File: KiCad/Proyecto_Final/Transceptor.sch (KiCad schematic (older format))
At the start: 51 parts, among them J2 ADC_CLK_SEL, T3 2450BL05A0100, U10 MAX2837, U9 MAX1193ETI+

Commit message: PCB MCU empezado.
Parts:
- added R13: 10k, Resistor_SMD:R_0402_1005Metric, symbol Device:R
- renumbered R13 to R14, R14 to R15, R15 to R16
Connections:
- net labels added: PD0_adc, PD1_adc
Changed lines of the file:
@@
 	4250 3150 4350 3150
 $Comp
-L power:GND #PWR070
+L power:GND #PWR071
 U 1 1 5FDBB07B
 P 4250 3250
-F 0 "#PWR070" H 4250 3000 50  0001 C CNN
+F 0 "#PWR071" H 4250 3000 50  0001 C CNN
 F 1 "GND" V 4255 3122 50  0000 R CNN
 F 2 "" H 4250 3250 50  0001 C CNN
@@
 	4250 3250 4350 3250
 $Comp
-L power:GND #PWR063
+L power:GND #PWR064
 U 1 1 5FDC599C
 P 1850 2750
-F 0 "#PWR063" H 1850 2500 50  0001 C CNN
+F 0 "#PWR064" H 1850 2500 50  0001 C CNN
 F 1 "GND" H 1855 2577 50  0000 C CNN
 F 2 "" H 1850 2750 50  0001 C CNN
@@
 $EndComp
 $Comp
-L power:GND #PWR067
+L power:GND #PWR068
 U 1 1 5FF7C6C8
 P 3850 2950
-F 0 "#PWR067" H 3850 2700 50  0001 C CNN
+F 0 "#PWR068" H 3850 2700 50  0001 C CNN
 F 1 "GND" H 3855 2777 50  0000 C CNN
 F 2 "" H 3850 2950 50  0001 C CNN
@@
 $EndComp
 $Comp
-L power:GND #PWR073
+L power:GND #PWR074
 U 1 1 602890BB
 P 3700 4100
-F 0 "#PWR073" H 3700 3850 50  0001 C CNN
+F 0 "#PWR074" H 3700 3850 50  0001 C CNN
 F 1 "GND" H 3705 3927 50  0000 C CNN
 F 2 "" H 3700 4100 50  0001 C CNN
@@
 	5650 5350 5650 5450
 $Comp
-L power:GND #PWR080
+L power:GND #PWR081
 U 1 1 602ED381
 P 5650 5950
-F 0 "#PWR080" H 5650 5700 50  0001 C CNN
+F 0 "#PWR081" H 5650 5700 50  0001 C CNN
 F 1 "GND" H 5655 5777 50  0000 C CNN
 F 2 "" H 5650 5950 50  0001 C CNN
@@
 $EndComp
 $Comp
-L power:GND #PWR081
+L power:GND #PWR082
 U 1 1 602F5473
 P 6050 5950
-F 0 "#PWR081" H 6050 5700 50  0001 C CNN
+F 0 "#PWR082" H 6050 5700 50  0001 C CNN
 F 1 "GND" H 6055 5777 50  0000 C CNN
 F 2 "" H 6050 5950 50  0001 C CNN
@@
 	6800 5450 6800 5500
 $Comp
-L power:GND #PWR082
+L power:GND #PWR083
 U 1 1 6030B87C
 P 6400 5950
-F 0 "#PWR082" H 6400 5700 50  0001 C CNN
+F 0 "#PWR083" H 6400 5700 50  0001 C CNN
 F 1 "GND" H 6405 5777 50  0000 C CNN
 F 2 "" H 6400 5950 50  0001 C CNN
@@
 	5700 5000 5700 5350
 $Comp
-L power:GND #PWR078
+L power:GND #PWR079
 U 1 1 6031E78A
 P 6000 5100
-F 0 "#PWR078" H 6000 4850 50  0001 C CNN
+F 0 "#PWR079" H 6000 4850 50  0001 C CNN
 F 1 "GND" H 6005 4927 50  0000 C CNN
 F 2 "" H 6000 5100 50  0001 C CNN
@@
 $EndComp
 $Comp
-L Device:R R14
+L Device:R R15
 U 1 1 603235A8
 P 7400 5450
-F 0 "R14" V 7193 5450 50  0000 C CNN
+F 0 "R15" V 7193 5450 50  0000 C CNN
 F 1 "475" V 7284 5450 50  0000 C CNN
 F 2 "Resistor_SMD:R_0402_1005Metric" V 7330 5450 50  0001 C CNN
@@
 $EndComp
 $Comp
-L Device:R R15
+L Device:R R16
 U 1 1 60324995
 P 7900 5450
-F 0 "R15" V 7693 5450 50  0000 C CNN
+F 0 "R16" V 7693 5450 50  0000 C CNN
 F 1 "475" V 7784 5450 50  0000 C CNN
 F 2 "Resistor_SMD:R_0402_1005Metric" V 7830 5450 50  0001 C CNN
@@
 Trx_Enable
 $Comp
-L power:GND #PWR076
+L power:GND #PWR077
 U 1 1 60342D46
 P 7100 4750
-F 0 "#PWR076" H 7100 4500 50  0001 C CNN
+F 0 "#PWR077" H 7100 4500 50  0001 C CNN
 F 1 "GND" H 7105 4577 50  0000 C CNN
 F 2 "" H 7100 4750 50  0001 C CNN
@@
 	7350 4050 6950 4050
 $Comp
-L power:GND #PWR075
+L power:GND #PWR076
 U 1 1 6034C833
 P 7350 4450
-F 0 "#PWR075" H 7350 4200 50  0001 C CNN
+F 0 "#PWR076" H 7350 4200 50  0001 C CNN
 F 1 "GND" H 7355 4277 50  0000 C CNN
 F 2 "" H 7350 4450 50  0001 C CNN
@@
 $EndComp
 $Comp
-L power:GND #PWR074
+L power:GND #PWR075
 U 1 1 6035D352
 P 7750 4250
-F 0 "#PWR074" H 7750 4000 50  0001 C CNN
+F 0 "#PWR075" H 7750 4000 50  0001 C CNN
 F 1 "GND" H 7755 4077 50  0000 C CNN
 F 2 "" H 7750 4250 50  0001 C CNN
@@
 $EndComp
 $Comp
-L power:GND #PWR069
+L power:GND #PWR070
 U 1 1 60414246
 P 11150 3100
-F 0 "#PWR069" H 11150 2850 50  0001 C CNN
+F 0 "#PWR070" H 11150 2850 50  0001 C CNN
 F 1 "GND" H 11155 2927 50  0000 C CNN
 F 2 "" H 11150 3100 50  0001 C CNN
@@
 	11400 3550 11500 3550
 $Comp
-L power:GND #PWR072
+L power:GND #PWR073
 U 1 1 60440365
 P 11700 3850
-F 0 "#PWR072" H 11700 3600 50  0001 C CNN
+F 0 "#PWR073" H 11700 3600 50  0001 C CNN
 F 1 "GND" H 11705 3677 50  0000 C CNN
 F 2 "" H 11700 3850 50  0001 C CNN
@@
 $EndComp
 $Comp
-L power:GND #PWR066
+L power:GND #PWR067
 U 1 1 604A2502
 P 15000 2850
-F 0 "#PWR066" H 15000 2600 50  0001 C CNN
+F 0 "#PWR067" H 15000 2600 50  0001 C CNN
 F 1 "GND" H 15005 2677 50  0000 C CNN
 F 2 "" H 15000 2850 50  0001 C CNN
@@
 $EndComp
 $Comp
-L power:GND #PWR071
+L power:GND #PWR072
 U 1 1 60506EB7
 P 14950 3250
-F 0 "#PWR071" H 14950 3000 50  0001 C CNN
+F 0 "#PWR072" H 14950 3000 50  0001 C CNN
 F 1 "GND" H 14955 3077 50  0000 C CNN
 F 2 "" H 14950 3250 50  0001 C CNN
@@
 CLK_ADC
 $Comp
-L power:GND #PWR064
+L power:GND #PWR065
 U 1 1 6030CF99
 P 4350 2800
-F 0 "#PWR064" H 4350 2550 50  0001 C CNN
+F 0 "#PWR065" H 4350 2550 50  0001 C CNN
 F 1 "GND" V 4355 2672 50  0000 R CNN
 F 2 "" H 4350 2800 50  0001 C CNN
@@
 Connection ~ 3700 3750
 $Comp
-L Device:R R13
+L Device:R R14
 U 1 1 60373025
 P 4000 4100
-F 0 "R13" H 4200 4100 50  0000 R CNN
+F 0 "R14" H 4200 4100 50  0000 R CNN
 F 1 "100" V 4000 4150 50  0000 R CNN
 F 2 "Resistor_SMD:R_0402_1005Metric" V 3930 4100 50  0001 C CNN
@@
 	5300 1100 5300 2400
 $Comp
-L power:GND #PWR065
+L power:GND #PWR066
 U 1 1 603671E8
 P 12300 2850
-F 0 "#PWR065" H 12300 2600 50  0001 C CNN
+F 0 "#PWR066" H 12300 2600 50  0001 C CNN
 F 1 "GND" V 12305 2677 50  0000 C CNN
 F 2 "" H 12300 2850 50  0001 C CNN
@@
 $EndComp
 $Comp
-L power:GND #PWR068
+L power:GND #PWR069
 U 1 1 60367BE1
 P 12300 2950
-F 0 "#PWR068" H 12300 2700 50  0001 C CNN
+F 0 "#PWR069" H 12300 2700 50  0001 C CNN
 F 1 "GND" V 12305 2777 50  0000 C CNN
 F 2 "" H 12300 2950 50  0001 C CNN
@@
 D0
 Text GLabel 13900 2650 2    50   Input ~ 0
-PD1
+PD1_adc
 Text GLabel 13900 2550 2    50   Input ~ 0
-PD0
+PD0_adc
 $Comp
 L power:GND #PWR057
@@
 $EndComp
 $Comp
-L power:GND #PWR079
+L power:GND #PWR080
 U 1 1 60757CE4
 P 4900 5400
-F 0 "#PWR079" H 4900 5150 50  0001 C CNN
+F 0 "#PWR080" H 4900 5150 50  0001 C CNN
 F 1 "GND" H 4905 5227 50  0000 C CNN
 F 2 "" H 4900 5400 50  0001 C CNN
@@
 VDD
 $Comp
-L power:+3.3V #PWR077
+L power:+3.3V #PWR078
 U 1 1 60750D11
 P 10500 5000
-F 0 "#PWR077" H 10500 4850 50  0001 C CNN
+F 0 "#PWR078" H 10500 4850 50  0001 C CNN
 F 1 "+3.3V" H 10515 5173 50  0000 C CNN
 F 2 "" H 10500 5000 50  0001 C CNN
@@
 Text Label 4100 3550 2    50   ~ 0
 RXRF-
+Text GLabel 8000 2900 3    50   Input ~ 0
+SPI1_CS1
+$Comp
+L Device:R R13
+U 1 1 60912B2D
+P 8000 2750
+F 0 "R13" H 8070 2796 50  0000 L CNN
+F 1 "10k" H 8070 2705 50  0000 L CNN
+F 2 "Resistor_SMD:R_0402_1005Metric" V 7930 2750 50  0001 C CNN
+F 3 "~" H 8000 2750 50  0001 C CNN
+	1    8000 2750
+	1    0    0    -1
+$EndComp
+$Comp
+L power:+3.3V #PWR063
+U 1 1 609150E8
+P 8000 2600
+F 0 "#PWR063" H 8000 2450 50  0001 C CNN
+F 1 "+3.3V" H 8015 2773 50  0000 C CNN
+F 2 "" H 8000 2600 50  0001 C CNN
+F 3 "" H 8000 2600 50  0001 C CNN
+	1    8000 2600
+	1    0    0    -1
+$EndComp
 $EndSCHEMATC

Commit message: Reasignación de footprints por cambio de proveedor de componentes (JLCPCB SMT Assembly).
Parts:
- C51: footprint Capacitor_SMD:C_0805_2012Metric -> Capacitor_SMD:C_0603_1608Metric
- C52, C54, C61, C64: value 0.1uF -> 100nF
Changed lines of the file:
@@
 P 11350 2200
 F 0 "C52" V 11098 2200 50  0000 C CNN
-F 1 "0.1uF" V 11189 2200 50  0000 C CNN
+F 1 "100nF" V 11189 2200 50  0000 C CNN
 F 2 "Capacitor_SMD:C_0402_1005Metric" H 11388 2050 50  0001 C CNN
 F 3 "~" H 11350 2200 50  0001 C CNN
@@
 F 0 "C51" V 10698 2200 50  0000 C CNN
 F 1 "2.2uF" V 10789 2200 50  0000 C CNN
-F 2 "Capacitor_SMD:C_0805_2012Metric" H 10988 2050 50  0001 C CNN
+F 2 "Capacitor_SMD:C_0603_1608Metric" H 10988 2050 50  0001 C CNN
 F 3 "~" H 10950 2200 50  0001 C CNN
 	1    10950 2200
@@
 P 11350 2950
 F 0 "C61" V 11098 2950 50  0000 C CNN
-F 1 "0.1uF" V 11189 2950 50  0000 C CNN
+F 1 "100nF" V 11189 2950 50  0000 C CNN
 F 2 "Capacitor_SMD:C_0402_1005Metric" H 11388 2800 50  0001 C CNN
 F 3 "~" H 11350 2950 50  0001 C CNN
@@
 P 11900 3700
 F 0 "C64" V 11648 3700 50  0000 C CNN
-F 1 "0.1uF" V 11739 3700 50  0000 C CNN
+F 1 "100nF" V 11739 3700 50  0000 C CNN
 F 2 "Capacitor_SMD:C_0402_1005Metric" H 11938 3550 50  0001 C CNN
 F 3 "~" H 11900 3700 50  0001 C CNN
@@
 P 15300 2200
 F 0 "C54" V 15048 2200 50  0000 C CNN
-F 1 "0.1uF" V 15139 2200 50  0000 C CNN
+F 1 "100nF" V 15139 2200 50  0000 C CNN
 F 2 "Capacitor_SMD:C_0402_1005Metric" H 15338 2050 50  0001 C CNN
 F 3 "~" H 15300 2200 50  0001 C CNN

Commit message: Sección RF terminada.
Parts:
- removed J2: ADC_CLK_SEL, Connector_PinHeader_2.54mm:PinHeader_2x02_P2.54mm_Vertical_SMD, symbol Connector_Generic:Conn_02x02_Counter_Clockwise
- removed R13: 10k, Resistor_SMD:R_0402_1005Metric, symbol Device:R
- renumbered R11 to R10, R12 to R11, R14 to R12, R15 to R13, R16 to R14, R8 to R7, R9 to R8, R10 to R9
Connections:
- net labels removed: ADC_22MHz, ADC_45MHz
- wire segments 148 -> 144

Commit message: Avances PCB.
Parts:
- renumbered C48 to C1, C57 to C10, C58 to C11, C59 to C12, C60 to C13, C61 to C14, C62 to C15, C63 to C16, C64 to C17, C65 to C18, C66 to C19, C49 to C2, C67 to C20, C68 to C21, C69 to C22, C70 to C23, C71 to C24, C72 to C25, C73 to C26, C74 to C27, C50 to C3, C51 to C4, C52 to C5, C53 to C6, C54 to C7, C55 to C8, C56 to C9, L4 to L1, R7 to R1, R8 to R2, R9 to R3, R10 to R4, R11 to R5, R12 to R6, R13 to R7, R14 to R8, T3 to T1, U9 to U1, U10 to U2

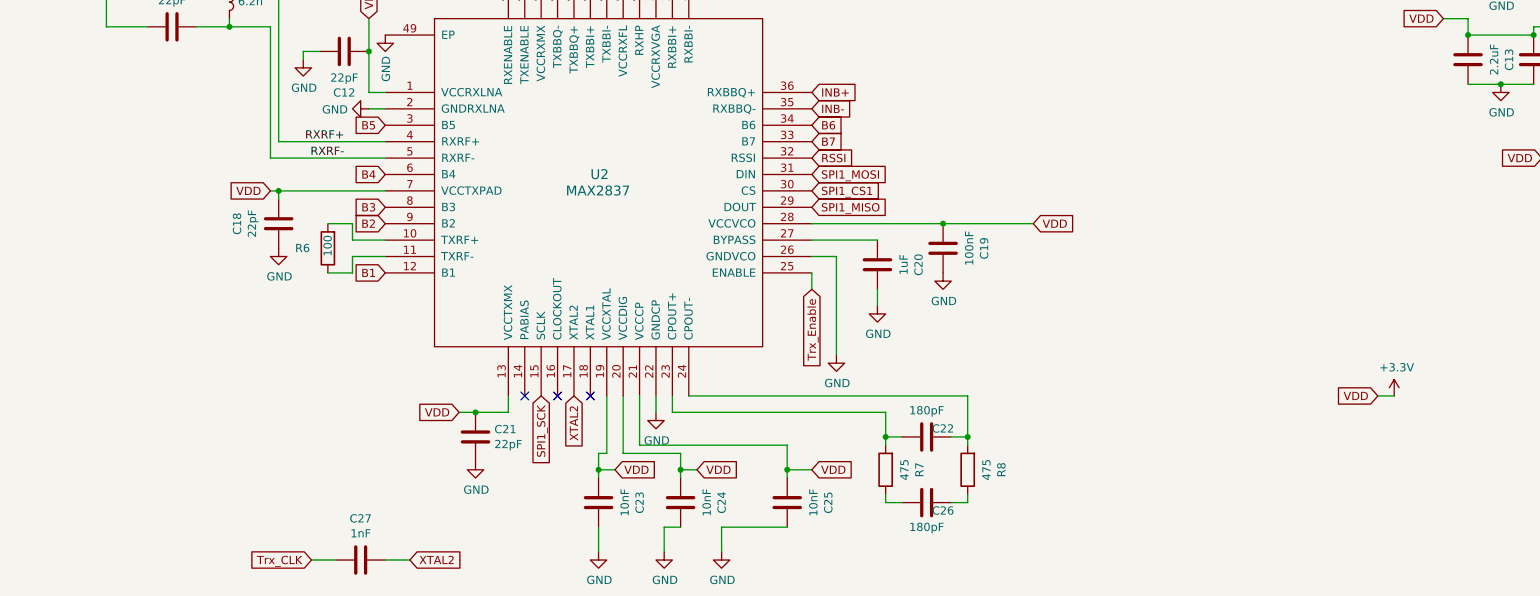
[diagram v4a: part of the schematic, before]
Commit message: Eliminadas conexiones innecesarias del transceptor.
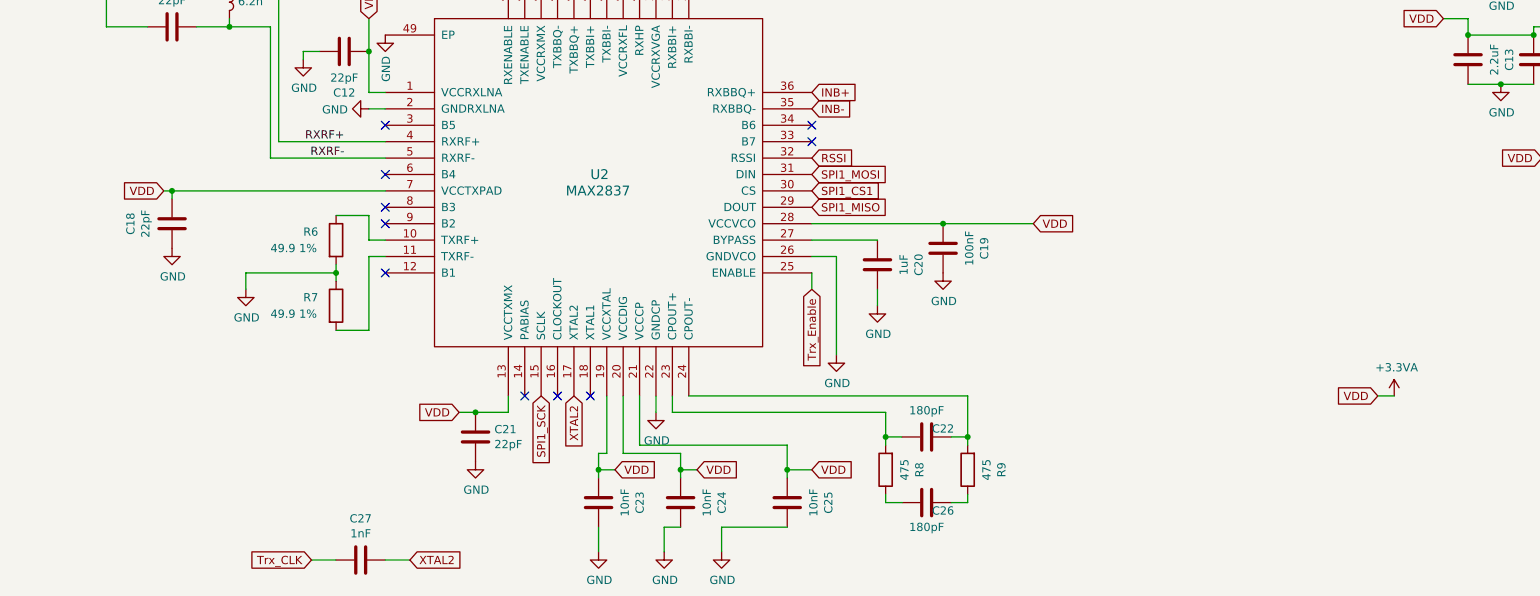
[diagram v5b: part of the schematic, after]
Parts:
- added R7: 49.9 1%, Resistor_SMD:R_0402_1005Metric, symbol Device:R
- R6: value 100 -> 49.9 1%
- renumbered R7 to R8, R8 to R9
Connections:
- net GND: now also R6.2, R7.1
- net at U2.10 (TXRF+): now also R6.1; no longer R6.2
- net at U2.11 (TXRF-): now also R7.2; no longer R6.1
- net +3V3 renamed +3.3VA
- net B1: no longer names the net of U2.12 (B1)
- net B2: no longer names the net of U2.9 (B2)
- net B3: no longer names the net of U2.8 (B3)
- net B4: no longer names the net of U2.6 (B4)
- net B5: no longer names the net of U2.3 (B5)
- net B6: no longer names the net of U2.34 (B6)
- net B7: no longer names the net of U2.33 (B7)
- no-connect marks 4 -> 11
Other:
- moved on the sheet: C18
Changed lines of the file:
@@
 L Device:C C18
 U 1 1 602785CE
-P 3700 3950
-F 0 "C18" V 3448 3950 50  0000 C CNN
-F 1 "22pF" V 3539 3950 50  0000 C CNN
-F 2 "Capacitor_SMD:C_0402_1005Metric" H 3738 3800 50  0001 C CNN
-F 3 "~" H 3700 3950 50  0001 C CNN
-	1    3700 3950
+P 3050 3950
+F 0 "C18" V 2798 3950 50  0000 C CNN
+F 1 "22pF" V 2889 3950 50  0000 C CNN
+F 2 "Capacitor_SMD:C_0402_1005Metric" H 3088 3800 50  0001 C CNN
+F 3 "~" H 3050 3950 50  0001 C CNN
+	1    3050 3950
 	1    0    0    -1
 $EndComp
@@
 L power:GND #PWR024
 U 1 1 602890BB
-P 3700 4100
-F 0 "#PWR024" H 3700 3850 50  0001 C CNN
-F 1 "GND" H 3705 3927 50  0000 C CNN
-F 2 "" H 3700 4100 50  0001 C CNN
-F 3 "" H 3700 4100 50  0001 C CNN
-	1    3700 4100
+P 3050 4100
+F 0 "#PWR024" H 3050 3850 50  0001 C CNN
+F 1 "GND" H 3055 3927 50  0000 C CNN
+F 2 "" H 3050 4100 50  0001 C CNN
+F 3 "" H 3050 4100 50  0001 C CNN
+	1    3050 4100
 	1    0    0    -1
 $EndComp
@@
 	5650 5350 5650 5450
 $Comp
-L power:GND #PWR031
+L power:GND #PWR032
 U 1 1 602ED381
 P 5650 5950
-F 0 "#PWR031" H 5650 5700 50  0001 C CNN
+F 0 "#PWR032" H 5650 5700 50  0001 C CNN
 F 1 "GND" H 5655 5777 50  0000 C CNN
 F 2 "" H 5650 5950 50  0001 C CNN
@@
 $EndComp
 $Comp
-L power:GND #PWR032
+L power:GND #PWR033
 U 1 1 602F5473
 P 6050 5950
-F 0 "#PWR032" H 6050 5700 50  0001 C CNN
+F 0 "#PWR033" H 6050 5700 50  0001 C CNN
 F 1 "GND" H 6055 5777 50  0000 C CNN
 F 2 "" H 6050 5950 50  0001 C CNN
@@
 	6800 5450 6800 5500
 $Comp
-L power:GND #PWR033
+L power:GND #PWR034
 U 1 1 6030B87C
 P 6400 5950
-F 0 "#PWR033" H 6400 5700 50  0001 C CNN
+F 0 "#PWR034" H 6400 5700 50  0001 C CNN
 F 1 "GND" H 6405 5777 50  0000 C CNN
 F 2 "" H 6400 5950 50  0001 C CNN
@@
 	5700 5000 5700 5350
 $Comp
-L power:GND #PWR029
+L power:GND #PWR030
 U 1 1 6031E78A
 P 6000 5100
-F 0 "#PWR029" H 6000 4850 50  0001 C CNN
+F 0 "#PWR030" H 6000 4850 50  0001 C CNN
 F 1 "GND" H 6005 4927 50  0000 C CNN
 F 2 "" H 6000 5100 50  0001 C CNN
@@
 $EndComp
 $Comp
-L Device:R R7
+L Device:R R8
 U 1 1 603235A8
 P 7400 5450
-F 0 "R7" V 7193 5450 50  0000 C CNN
+F 0 "R8" V 7193 5450 50  0000 C CNN
 F 1 "475" V 7284 5450 50  0000 C CNN
 F 2 "Resistor_SMD:R_0402_1005Metric" V 7330 5450 50  0001 C CNN
@@
 $EndComp
 $Comp
-L Device:R R8
+L Device:R R9
 U 1 1 60324995
 P 7900 5450
-F 0 "R8" V 7693 5450 50  0000 C CNN
+F 0 "R9" V 7693 5450 50  0000 C CNN
 F 1 "475" V 7784 5450 50  0000 C CNN
 F 2 "Resistor_SMD:R_0402_1005Metric" V 7830 5450 50  0001 C CNN
@@
 Trx_Enable
 $Comp
-L power:GND #PWR027
+L power:GND #PWR028
 U 1 1 60342D46
 P 7100 4750
-F 0 "#PWR027" H 7100 4500 50  0001 C CNN
+F 0 "#PWR028" H 7100 4500 50  0001 C CNN
 F 1 "GND" H 7105 4577 50  0000 C CNN
 F 2 "" H 7100 4750 50  0001 C CNN
@@
 	7350 4050 6950 4050
 $Comp
-L power:GND #PWR026
+L power:GND #PWR027
 U 1 1 6034C833
 P 7350 4450
-F 0 "#PWR026" H 7350 4200 50  0001 C CNN
+F 0 "#PWR027" H 7350 4200 50  0001 C CNN
 F 1 "GND" H 7355 4277 50  0000 C CNN
 F 2 "" H 7350 4450 50  0001 C CNN
@@
 	1    0    0    -1
 $EndComp
-Text GLabel 3650 3750 0    50   Input ~ 0
+Text GLabel 3000 3750 0    50   Input ~ 0
 VDD
 Text GLabel 4250 2700 1    50   Input ~ 0
@@
 Connection ~ 4250 2900
 Wire Wire Line
-	3650 3750 3700 3750
-Wire Wire Line
-	3700 3800 3700 3750
-Connection ~ 3700 3750
-$Comp
-L Device:R R6
-U 1 1 60373025
-P 4000 4100
-F 0 "R6" H 4200 4100 50  0000 R CNN
-F 1 "100" V 4000 4150 50  0000 R CNN
-F 2 "Resistor_SMD:R_0402_1005Metric" V 3930 4100 50  0001 C CNN
-F 3 "~" H 4000 4100 50  0001 C CNN
-	1    4000 4100
-	-1   0    0    1
-$EndComp
+	3000 3750 3050 3750
+Wire Wire Line
+	3050 3800 3050 3750
+Connection ~ 3050 3750
 NoConn ~ 5200 5000
 $Comp
@@
 $EndComp
 $Comp
-L power:GND #PWR030
+L power:GND #PWR031
 U 1 1 60757CE4
 P 4900 5400
-F 0 "#PWR030" H 4900 5150 50  0001 C CNN
+F 0 "#PWR031" H 4900 5150 50  0001 C CNN
 F 1 "GND" H 4905 5227 50  0000 C CNN
 F 2 "" H 4900 5400 50  0001 C CNN
@@
 Text GLabel 5900 2400 1    50   Input ~ 0
 RXHP
-Text GLabel 4350 3350 0    50   Input ~ 0
-B5
-Text GLabel 4350 3650 0    50   Input ~ 0
-B4
-Text GLabel 4350 3850 0    50   Input ~ 0
-B3
-Text GLabel 4350 3950 0    50   Input ~ 0
-B2
-Wire Wire Line
-	3700 3750 4350 3750
-Wire Wire Line
-	4350 4050 4150 4050
-Wire Wire Line
-	4150 4050 4150 3950
-Wire Wire Line
-	4150 3950 4000 3950
-Wire Wire Line
-	4350 4150 4150 4150
-Wire Wire Line
-	4150 4150 4150 4250
-Wire Wire Line
-	4150 4250 4000 4250
-Text GLabel 4350 4250 0    50   Input ~ 0
-B1
-Text GLabel 6950 3350 2    50   Input ~ 0
-B6
-Text GLabel 6950 3450 2    50   Input ~ 0
-B7
 Wire Wire Line
 	6000 1650 6450 1650
@@
 Text GLabel 10400 5000 0    50   Input ~ 0
 VDD
-$Comp
-L power:+3.3V #PWR028
-U 1 1 60750D11
-P 10500 5000
-F 0 "#PWR028" H 10500 4850 50  0001 C CNN
-F 1 "+3.3V" H 10515 5173 50  0000 C CNN
-F 2 "" H 10500 5000 50  0001 C CNN
-F 3 "" H 10500 5000 50  0001 C CNN
-	1    10500 5000
-	1    0    0    -1
-$EndComp
 Wire Wire Line
 	10400 5000 10500 5000
@@
 Text Label 4100 3550 2    50   ~ 0
 RXRF-
+NoConn ~ 4350 3350
+NoConn ~ 4350 3650
+NoConn ~ 4350 3850
+NoConn ~ 4350 3950
+NoConn ~ 4350 4250
+NoConn ~ 6950 3350
+NoConn ~ 6950 3450
+$Comp
+L Device:R R6
+U 1 1 609C17D5
+P 4050 4050
+F 0 "R6" H 3850 4100 50  0000 L CNN
+F 1 "49.9 1%" H 3650 4000 50  0000 L CNN
+F 2 "Resistor_SMD:R_0402_1005Metric" V 3980 4050 50  0001 C CNN
+F 3 "~" H 4050 4050 50  0001 C CNN
+	1    4050 4050
+	1    0    0    -1
+$EndComp
+$Comp
+L Device:R R7
+U 1 1 609C1B2A
+P 4050 4450
+F 0 "R7" H 3850 4500 50  0000 L CNN
+F 1 "49.9 1%" H 3650 4400 50  0000 L CNN
+F 2 "Resistor_SMD:R_0402_1005Metric" V 3980 4450 50  0001 C CNN
+F 3 "~" H 4050 4450 50  0001 C CNN
+	1    4050 4450
+	1    0    0    -1
+$EndComp
+Wire Wire Line
+	4050 4200 4050 4250
+Wire Wire Line
+	3050 3750 4350 3750
+Wire Wire Line
+	4350 4050 4250 4050
+Wire Wire Line
+	4250 4050 4250 3900
+Wire Wire Line
+	4250 3900 4050 3900
+Wire Wire Line
+	4350 4150 4250 4150
+Wire Wire Line
+	4250 4150 4250 4600
+Wire Wire Line
+	4250 4600 4050 4600
+$Comp
+L power:GND #PWR026
+U 1 1 609E6CD2
+P 3500 4350
+F 0 "#PWR026" H 3500 4100 50  0001 C CNN
+F 1 "GND" H 3505 4177 50  0000 C CNN
+F 2 "" H 3500 4350 50  0001 C CNN
+F 3 "" H 3500 4350 50  0001 C CNN
+	1    3500 4350
+	1    0    0    -1
+$EndComp
+Wire Wire Line
+	3500 4350 3500 4250
+Wire Wire Line
+	3500 4250 4050 4250
+Connection ~ 4050 4250
+Wire Wire Line
+	4050 4250 4050 4300
+$Comp
+L power:+3.3VA #PWR?
+U 1 1 60A0F8F4
+P 10500 5000
+F 0 "#PWR?" H 10500 4850 50  0001 C CNN
+F 1 "+3.3VA" H 10515 5173 50  0000 C CNN
+F 2 "" H 10500 5000 50  0001 C CNN
+F 3 "" H 10500 5000 50  0001 C CNN
+	1    10500 5000
+	1    0    0    -1
+$EndComp
 $EndSCHEMATC
